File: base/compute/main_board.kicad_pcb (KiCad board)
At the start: 2 copper layers, 54.4 x 37.6 mm, 41 parts, among them J1 USB_C_Receptacle_USB2.0_16P, J2 Conn_01x20, J4 Conn_01x20, SW1 SW_Push_Open, U1 MCP1700T-1202ETT, U2 ESP32-S3-WROOM-2, U3 MCP1700T-3302E/TT, U4 W25X20CLSN, U5 ICE40UP5K-SG48ITR-FPGA_Lattice

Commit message: compute  module ready for fab
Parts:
- removed H3, H4: MountingHole, MountingHole:MountingHole_2.7mm_M2.5
- added H1: MountingHole, MountingHole:MountingHole_3.2mm_M3, F.Cu at (227.0, 139.0)
- added H2: MountingHole, MountingHole:MountingHole_3.2mm_M3, F.Cu at (200.0, 163.0)
- added SW2: SW_Push_Open, Button_Switch_SMD:SW_SPST_B3U-1000P, F.Cu at (192.6, 158.2)
- J1: footprint Connector_USB:USB_C_Receptacle_GCT_USB4105-xx-A_16P_TopMnt_Horizontal -> footprints:USB_C_Receptacle_GCT_USB4105-xx-A_16P_TopMnt_Horizontal
- J2, J4, U2: moved to F.Cu
- SW1: footprint footprints:SW_SPST_CK_KXT3 -> Button_Switch_SMD:SW_SPST_B3U-1000P
- U3: value MCP1700T-3302E/TT -> LD1117S33TR_SOT223; footprint Package_TO_SOT_SMD:SOT-23 -> Package_TO_SOT_SMD:SOT-223-3_TabPin2
- U5: footprint Package_DFN_QFN:QFN-48-1EP_7x7mm_P0.5mm_EP5.6x5.6mm -> footprints:QFN-48-1EP_7x7mm_P0.5mm_EP5.6x5.6mm
- moved C10 47.2 mm to (229.8, 155.8), turned to 90 degrees
- moved C2 47.0 mm to (226.7, 150.8), turned to 180 degrees
- moved U3 43.9 mm to (227.1, 162.6)
- moved C1 34.6 mm to (221.1, 161.9), turned to 0 degrees
- moved R10 32.5 mm to (206.5, 157.3)
- moved SW1 28.8 mm to (205.9, 137.8)
- moved U2 23.1 mm to (193.4, 145.4)
- moved C13 20.8 mm to (206.5, 155.2)
- moved R6 20.0 mm to (188.3, 161.0), turned to 0 degrees
- moved C14 18.9 mm to (206.5, 153.1)
- moved J1 17.2 mm to (181.1, 160.9)
- moved D2 16.8 mm to (212.8, 164.2)
- moved D3 15.5 mm to (191.1, 163.5)
- moved D1 14.4 mm to (207.8, 150.2), turned to 0 degrees
- moved U1 14.4 mm to (226.7, 153.7)
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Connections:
- C12 pad 1: +3V3 -> +3.3V
- C2 pad 1: +5V -> +3.3V
- C3 pad 1: +3V3 -> +3.3V
- C4 pad 1: +3V3 -> +3.3V
- C5 pad 1: +3V3 -> +3.3V
- C6 pad 1: +3V3 -> +3.3V
- C7 pad 1: +3V3 -> +3.3V
- C8 pad 1: +3V3 -> +3.3V
- D1 pad 2: +3V3 -> +3.3V
- D2 pad 1: +3V3 -> +3.3V
- J2 pad 10: SPI_SI -> HALL1
- J2 pad 11: SPI_SCK -> HALL2
- J2 pad 12: IC_HB_PWM1 -> HALL3
- J2 pad 13: IC_HB_PWM2 -> uH
- J2 pad 14: STEP_ENABLE -> uL
- J2 pad 15: POT_SCL -> vH
- J2 pad 16: POT_SDA -> vL
- J2 pad 17: FPGA36 -> wH
- J2 pad 18: FPGA37 -> wL
- J2 pad 19: FPGA46 -> IC_HB_PWM1
- J2 pad 2: uL -> POT_SDA
- J2 pad 20: FPGA48 -> IC_HB_PWM2
- J2 pad 3: uH -> POT_SCL
- J2 pad 4: vL -> GPIO21
- J2 pad 5: vL -> FPGA42
- J2 pad 6: wL -> FPGA43
- J2 pad 7: wH -> FPGA44
- J2 pad 8: SPI_SS_MOTOR -> FPGA46
- J2 pad 9: SPI_SO -> DIGITAL
- J4 pad 1: vH -> GND
- J4 pad 10: Z_PO -> SPI_SO
- J4 pad 11: Z_STEP -> SPI_SI
- J4 pad 12: Y_DIR -> Z_PO
- J4 pad 13: Y_PO -> Z_STEP
- J4 pad 14: Y_STEP -> Z_DIR
- J4 pad 15: X_DIR -> Y_PO
- J4 pad 16: X_PO -> Y_STEP
- J4 pad 17: X_STEP -> Y_DIR
- J4 pad 18: SPI_SO -> X_PO
- J4 pad 19: SPI_SI -> X_STEP
- J4 pad 2: HALL3 -> GPIO44
- J4 pad 20: GND -> X_DIR
- J4 pad 3: HALL1 -> GPIO43
- J4 pad 4: HALL2 -> FPGA41
- J4 pad 5: DIGITAL -> FPGA38
- J4 pad 6: FREE -> FPGA39
- J4 pad 7: FPGA51 -> STEP_ENABLE
- J4 pad 8: FPGA50 -> SPI_SS_MOTOR
- J4 pad 9: Z_DIR -> SPI_SCK
- R1 pad 1: +3V3 -> +3.3V
- R2 pad 1: +3V3 -> +3.3V
- R3 pad 2: +3V3 -> +3.3V
- R7 pad 1: +3V3 -> +3.3V
- U1 pad 3: +3V3 -> +3.3V
- U2 pad 12: unconnected-(U2-GPIO8/TOUCH8/ADC1_CH7/SUBSPICS1-Pad12) -> ESP32_RED
- U2 pad 15: unconnected-(U2-GPIO3/TOUCH3/ADC1_CH2-Pad15) -> FPGA41
- U2 pad 17: STEP_ENABLE -> SPI_SS_FPGA
- U2 pad 18: POT_SCL -> SPI_SS
- U2 pad 22: unconnected-(U2-GPIO14/TOUCH14/ADC2_CH3/FSPIWP/FSPIDQS/SUBSPIWP-Pad22) -> SPI_SS_MOTOR
- U2 pad 23: ESP32_RED -> GPIO21
- U2 pad 25: POT_SDA -> CFG_DONE
- U2 pad 26: SPI_SS_FPGA -> unconnected-(U2-GPIO45-Pad26)
- U2 pad 31: CFG_DONE -> STEP_ENABLE
- U2 pad 32: FREE -> unconnected-(U2-MTCK/GPIO39/CLK_OUT3/SUBSPICS1-Pad32)
- U2 pad 35: SPI_SS_MOTOR -> unconnected-(U2-MTMS/GPIO42-Pad35)
- U2 pad 36: unconnected-(U2-U0RXD/GPIO44/CLK_OUT2-Pad36) -> GPIO44
- U2 pad 37: Z_STEP -> GPIO43
- U2 pad 38: unconnected-(U2-GPIO2/TOUCH2/ADC1_CH1-Pad38) -> FPGA39
- U2 pad 39: unconnected-(U2-GPIO1/TOUCH1/ADC1_CH0-Pad39) -> FPGA38
- U2 pad 4: unconnected-(U2-GPIO4/TOUCH4/ADC1_CH3-Pad4) -> POT_SDA
- U2 pad 5: unconnected-(U2-GPIO5/TOUCH5/ADC1_CH4-Pad5) -> POT_SCL
- U2 pad 6: unconnected-(U2-GPIO6/TOUCH6/ADC1_CH5-Pad6) -> FPGA46
- U2 pad 7: unconnected-(U2-GPIO7/TOUCH7/ADC1_CH6-Pad7) -> FPGA44
- U2 pad 8: unconnected-(U2-GPIO15/U0RTS/ADC2_CH4/XTAL_32K_P-Pad8) -> FPGA42
- U2 pad 9: unconnected-(U2-GPIO16/U0CTS/ADC2_CH5/XTAL_32K_N-Pad9) -> FPGA43
- U4 pad 8: +3V3 -> +3.3V
- U5 pad 1: +3V3 -> +3.3V
- U5 pad 10: SPI_SS_FPGA -> Y_DIR
- U5 pad 11: Y_PO -> Y_STEP
- U5 pad 12: Y_STEP -> Y_PO
- U5 pad 20: Z_PO -> Z_DIR
- U5 pad 21: Y_DIR -> Z_STEP
- U5 pad 22: +3V3 -> +3.3V
- U5 pad 23: FPGA37 -> Z_PO
- U5 pad 25: FPGA36 -> SPI_SS_FPGA
- U5 pad 26: FREE -> FPGA39
- U5 pad 27: Z_STEP -> FPGA38
- U5 pad 28: Z_DIR -> FPGA41
- U5 pad 31: DIGITAL -> FPGA42
- U5 pad 32: HALL2 -> FPGA43
- U5 pad 33: +3V3 -> +3.3V
- U5 pad 34: HALL1 -> FPGA44
- U5 pad 36: FPGA48 -> DIGITAL
- U5 pad 37: HALL3 -> HALL1
- U5 pad 38: FPGA50 -> HALL2
- U5 pad 42: FPGA51 -> HALL3
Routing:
- net +3.3V: track 0.00 -> 149.1 mm, vias 0 -> 8
- net +3V3: track 123.5 -> 0.00 mm, vias 10 -> 0
- net +5V: track 0.00 -> 55.6 mm
- net FPGA44: track 0.00 -> 47.0 mm, vias 0 -> 1
- net FPGA41: track 0.00 -> 43.7 mm, vias 0 -> 1
- net FPGA43: track 0.00 -> 40.5 mm, vias 0 -> 2
- net FPGA38: track 0.00 -> 37.9 mm, vias 0 -> 1
- net FPGA39: track 0.00 -> 37.5 mm, vias 0 -> 1
- net FPGA42: track 0.00 -> 36.7 mm, vias 0 -> 2
- net FPGA46: track 14.9 -> 50.2 mm, vias 0 -> 1
- net GPIO21: track 0.00 -> 34.0 mm, vias 0 -> 1
- net X_STEP: track 0.00 -> 32.3 mm
- net +1V2: track 62.5 -> 30.8 mm
- net D+: track 0.00 -> 31.3 mm
- net X_PO: track 0.00 -> 30.9 mm
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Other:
- board size 54.4 x 37.6 mm -> 53.8 x 41.5 mm
- board text added: "BOOT"
- board text added: "EN"
- board text removed: "RASPBERRY-PI 40-PIN ADDON BOARD VIEW FROM TOP NOTE: P1 SHOULD BE FITTED ON THE REVERSE OF THE BOARD ADD EDGE CUTS FROM CAMERA AND DISPLAY PORTS AS REQUIRED"
- board text removed: "RJ45"
- board text removed: "USB"

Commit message: changes for extension
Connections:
- J2 pad 2: POT_SDA -> +3.3V
- J2 pad 3: POT_SCL -> POT_SDA
- J2 pad 4: GPIO21 -> POT_SCL
- U2 pad 23: GPIO21 -> unconnected-(U2-GPIO21-Pad23)
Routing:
- net GPIO21: track 34.0 -> 0.00 mm, vias 1 -> 0
- net +3.3V: track 149.1 -> 167.4 mm
- net POT_SDA: track 17.2 -> 16.4 mm
- net POT_SCL: track 16.3 -> 16.8 mm, vias 1 -> 2
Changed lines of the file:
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@@
 	(net 75 "GPIO43")
 	(net 76 "GPIO44")
-	(net 77 "GPIO21")
+	(net 77 "unconnected-(U2-GPIO21-Pad23)")
 	(footprint "Package_TO_SOT_SMD:SOT-23"
 		(layer "F.Cu")
@@
 			(size 1.5 0.9)
 			(layers "F.Cu" "F.Paste" "F.Mask")
-			(net 77 "GPIO21")
+			(net 77 "unconnected-(U2-GPIO21-Pad23)")
 			(pinfunction "GPIO21")
-			(pintype "bidirectional")
+			(pintype "bidirectional+no_connect")
 		)
 		(pad "24" smd rect
@@
 			(layers "*.Cu" "*.Mask")
 			(remove_unused_layers no)
-			(net 9 "POT_SDA")
+			(net 3 "+3.3V")
 			(pinfunction "Pin_2")
 			(pintype "passive")
@@
 			(layers "*.Cu" "*.Mask")
 			(remove_unused_layers no)
-			(net 11 "POT_SCL")
+			(net 9 "POT_SDA")
 			(pinfunction "Pin_3")
 			(pintype "passive")
@@
 			(layers "*.Cu" "*.Mask")
 			(remove_unused_layers no)
-			(net 77 "GPIO21")
+			(net 11 "POT_SCL")
 			(pinfunction "Pin_4")
 			(pintype "passive")
@@
 	)
 	(segment
+		(start 190.09 157.9)
+		(end 197.1375 157.9)
+		(width 0.25)
+		(layer "F.Cu")
+		(net 3)
+	)
+	(segment
 		(start 188.645 156.36061)
 		(end 188.645 157.44)
@@
 	)
 	(segment
+		(start 190.09 157.9)
+		(end 190.09 162.47061)
+		(width 0.25)
+		(layer "F.Cu")
+		(net 3)
+	)
+	(segment
+		(start 185.136555 166.403445)
+		(end 190.263445 166.403445)
+		(width 0.25)
+		(layer "F.Cu")
+		(net 3)
+	)
+	(segment
 		(start 206.4875 160.18)
 		(end 208.328626 160.18)
@@
 	)
 	(segment
+		(start 182.54 169)
+		(end 185.136555 166.403445)
+		(width 0.25)
+		(layer "F.Cu")
+		(net 3)
+	)
+	(segment
 		(start 220.0125 161.96)
 		(end 220.0125 164)
@@
 	)
 	(segment
+		(start 190.71 163.09061)
+		(end 190.71 165.95689)
+		(width 0.25)
+		(layer "F.Cu")
+		(net 3)
+	)
+	(segment
+		(start 190.71 165.95689)
+		(end 190.263445 166.403445)
+		(width 0.25)
+		(layer "F.Cu")
+		(net 3)
+	)
+	(segment
 		(start 219.5075 139.5)
 		(end 219.5075 139.46)
@@
 	)
 	(segment
+		(start 190.09 162.47061)
+		(end 190.71 163.09061)
+		(width 0.25)
+		(layer "F.Cu")
+		(net 3)
+	)
+	(segment
 		(start 214.0165 153.244526)
 		(end 214.0165 152.51)
@@
 	)
 	(segment
-		(start 189.105 157.9)
-		(end 197.1375 157.9)
-		(width 0.25)
-		(layer "F.Cu")
-		(net 3)
-	)
-	(segment
 		(start 214.0165 151.6535)
 		(end 213.5 151.137)
@@
 	)
 	(segment
+		(start 189.105 157.9)
+		(end 190.09 157.9)
+		(width 0.25)
+		(layer "F.Cu")
+		(net 3)
+	)
+	(segment
 		(start 228.1275 153.7375)
 		(end 228.07 153.68)
@@
 	)
 	(segment
+		(start 182.54 168.448652)
+		(end 183.127364 168.448652)
+		(width 0.25)
+		(layer "B.Cu")
+		(net 3)
+	)
+	(segment
 		(start 215.935 148.135)
 		(end 220.98 143.09)
@@
 	)
 	(segment
-		(start 182.54 168.448652)
-		(end 183.127364 168.448652)
+		(start 185.93 168.15)
+		(end 185.93 157.2)
 		(width 0.25)
 		(layer "B.Cu")
@@
 	)
 	(segment
-		(start 183.127364 168.448652)
-		(end 188.92 162.656016)
+		(start 185.08 169)
+		(end 185.93 168.15)
 		(width 0.25)
 		(layer "B.Cu")
@@
 	)
 	(segment
-		(start 188.92 162.656016)
+		(start 185.93 157.2)
 		(end 188.92 154.21)
 		(width 0.25)
@@
 		(net 10)
 	)
+	(segment
+		(start 186.63 166.98)
+		(end 186.63 168.01)
+		(width 0.25)
+		(layer "F.Cu")
+		(net 11)
+	)
+	(segment
+		(start 186.63 168.01)
+		(end 187.62 169)
+		(width 0.25)
+		(layer "F.Cu")
+		(net 11)
+	)
+	(via
+		(at 186.63 166.98)
+		(size 0.6)
+		(drill 0.4)
+		(layers "F.Cu" "B.Cu")
+		(net 11)
+	)
 	(via
 		(at 190.19 154.22)
@@
 	)
 	(segment
-		(start 185.08 168.448652)
-		(end 189.32 164.208652)
+		(start 186.63 166.9)
+		(end 186.63 166.98)
 		(width 0.25)
 		(layer "B.Cu")
@@
 	)
 	(segment
+		(start 189.32 164.208652)
+		(end 187.45 166.078652)
+		(width 0.25)
+		(layer "B.Cu")
+		(net 11)
+	)
+	(segment
+		(start 187.45 166.08)
+		(end 186.63 166.9)
+		(width 0.25)
+		(layer "B.Cu")
+		(net 11)
+	)
+	(segment
+		(start 186.63 166.98)
+		(end 186.55 166.98)
+		(width 0.25)
+		(layer "B.Cu")
+		(net 11)
+	)
+	(segment
+		(start 186.55 166.98)
+		(end 186.61 166.92)
+		(width 0.25)
+		(layer "B.Cu")
+		(net 11)
+	)
+	(segment
+		(start 187.45 166.078652)
+		(end 187.45 166.08)
+		(width 0.25)
+		(layer "B.Cu")
+		(net 11)
+	)
+	(segment
 		(start 215.66 140.65)
 		(end 212.505686 140.65)
@@
 	)
 	(segment
-		(start 189.4025 166.015)
+		(start 189.414055 166.003445)
 		(end 189.8775 165.54)
 		(width 0.25)
@@
 	(segment
 		(start 180 168.448652)
-		(end 182.433652 166.015)
+		(end 182.445207 166.003445)
 		(width 0.25)
 		(layer "F.Cu")
@@
 	)
 	(segment
-		(start 182.433652 166.015)
-		(end 189.4025 166.015)
+		(start 182.445207 166.003445)
+		(end 189.414055 166.003445)
 		(width 0.25)
 		(layer "F.Cu")
@@
 	(segment
 		(start 187.559009 170.53)
-		(end 186.495 169.465991)
+		(end 196.25 170.53)
 		(width 0.25)
 		(layer "B.Cu")
@@
 	)
 	(segment
-		(start 197.78 169)
-		(end 196.25 170.53)
+		(start 189.72 155.874952)
+		(end 189.72 164.434314)
 		(width 0.25)
 		(layer "B.Cu")
@@
 	)
 	(segment
-		(start 186.495 167.620685)
-		(end 189.72 164.395685)
+		(start 189.74 164.454314)
+		(end 189.74 165.289009)
 		(width 0.25)
 		(layer "B.Cu")
@@
 	)
 	(segment
-		(start 189.72 164.395685)
-		(end 189.72 155.874952)
+		(start 186.495 169.465991)
+		(end 187.559009 170.53)
+		(width 0.25)
+		(layer "B.Cu")
+		(net 65)
+	)
+	(segment
+		(start 186.495 168.534009)
+		(end 186.495 169.465991)
 		(width 0.25)
 		(layer "B.Cu")
@@
 	(segment
 		(start 196.25 170.53)
-		(end 187.559009 170.53)
+		(end 197.78 169)
 		(width 0.25)
 		(layer "B.Cu")
@@
 	)
 	(segment
-		(start 189.72 155.874952)
-		(end 191.347842 154.24711)
+		(start 189.72 164.434314)
+		(end 189.74 164.454314)
 		(width 0.25)
 		(layer "B.Cu")
@@
 	)
 	(segment
-		(start 186.495 169.465991)
-		(end 186.495 167.620685)
+		(start 189.74 165.289009)
+		(end 186.495 168.534009)
+		(width 0.25)
+		(layer "B.Cu")
+		(net 65)
+	)
+	(segment
+		(start 191.347842 154.24711)
+		(end 189.72 155.874952)
 		(width 0.25)
 		(layer "B.Cu")
@@
 		(net 76)
 	)
-	(segment
-		(start 195.83 148.23)
-		(end 195.8 148.21)
-		(width 0.25)
-		(layer "F.Cu")
-		(net 77)
-	)
-	(segment
-		(start 201.37 142.235)
-		(end 195.8 147.805)
-		(width 0.25)
-		(layer "F.Cu")
-		(net 77)
-	)
-	(segment
-		(start 195.8 147.805)
-		(end 195.83 148.23)
-		(width 0.25)
-		(layer "F.Cu")
-		(net 77)
-	)
-	(segment
-		(start 202.88 142.235)
-		(end 201.37 142.235)
-		(width 0.25)
-		(layer "F.Cu")
-		(net 77)
-	)
-	(via
-		(at 195.83 148.23)
-		(size 0.6)
-		(drill 0.4)
-		(layers "F.Cu" "B.Cu")
-		(net 77)
-	)
-	(segment
-		(start 192.526587 164.093413)
-		(end 192.526587 151.533413)
-		(width 0.25)
-		(layer "B.Cu")
-		(net 77)
-	)
-	(segment
-		(start 192.526587 151.533413)
-		(end 195.83 148.23)
-		(width 0.25)
-		(layer "B.Cu")
-		(net 77)
-	)
-	(segment
-		(start 187.62 169)
-		(end 192.526587 164.093413)
-		(width 0.25)
-		(layer "B.Cu")
-		(net 77)
-	)
 	(zone

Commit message: improved layout main board
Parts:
- added R8: 10K, Resistor_SMD:R_0805_2012Metric, F.Cu at (192.2, 155.0)
- added R9: 10K, Resistor_SMD:R_0805_2012Metric, F.Cu at (192.2, 157.2)
- G1: moved to F.Cu
- moved SW2 45.1 mm to (234.5, 141.6), turned to 0 degrees
- moved D4 35.4 mm to (235.5, 153.9), turned to -90 degrees
- moved D2 29.3 mm to (235.5, 145.6), turned to -90 degrees
- moved SW1 28.6 mm to (234.5, 137.8), turned to 0 degrees
- moved H2 26.1 mm to (174.5, 168.5)
- moved C10 11.6 mm to (226.9, 167.0), turned to 180 degrees
- moved H1 10.3 mm to (234.0, 131.5)
- moved R4 9.70 mm to (188.4, 155.0), turned to 180 degrees
- moved G1 8.46 mm to (205.6, 133.8), turned to 0 degrees
- moved U2 7.16 mm to (187.1, 142.0)
- moved J1 6.53 mm to (174.7, 159.3)
- moved F2 6.44 mm to (188.7, 163.8)
- moved C9 6.29 mm to (182.4, 155.0)
- moved D3 6.29 mm to (185.1, 161.8)
- moved D5 6.29 mm to (185.1, 163.9)
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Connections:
- C11 pad 1: +3.3V -> +1V2
- J2 pad 2: +3.3V -> GPIO46
- J2 pad 5: FPGA42 -> FPGA44
- J2 pad 6: FPGA43 -> FPGA42
- J2 pad 7: FPGA44 -> FPGA43
- U2 pad 16: unconnected-(U2-GPIO46-Pad16) -> GPIO46
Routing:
- net Net-(U2-EN): track 12.2 -> 76.0 mm, vias 0 -> 2
- net ESP32_BLUE: track 4.83 -> 56.1 mm, vias 0 -> 2
- net ESP32_GREEN: track 4.76 -> 53.4 mm, vias 0 -> 2
- net ESP32_RED: track 6.32 -> 52.1 mm, vias 0 -> 2
- net FPGAG: track 4.43 -> 47.5 mm, vias 0 -> 2
- net Net-(U2-GPIO0/BOOT): track 4.51 -> 47.2 mm
- net GPIO46: track 0.00 -> 36.9 mm, vias 0 -> 1
- net FPGAB: track 3.91 -> 39.6 mm, vias 0 -> 2
- net FPGAR: track 8.13 -> 33.3 mm, vias 0 -> 2
- net POT_SCL: track 16.8 -> 35.8 mm, vias 2 -> 1
- net POT_SDA: track 16.4 -> 33.1 mm
- net SPI_SS_MOTOR: track 20.6 -> 10.8 mm
- net FPGA41: track 43.7 -> 52.7 mm
- net FPGA38: track 37.9 -> 46.3 mm
- net FPGA43: track 40.5 -> 48.8 mm
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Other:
- board size 53.8 x 41.5 mm -> 66.5 x 44 mm
- board text added: "ESP32"
- board text added: "FPGA"
- board text added: "version 0.1"

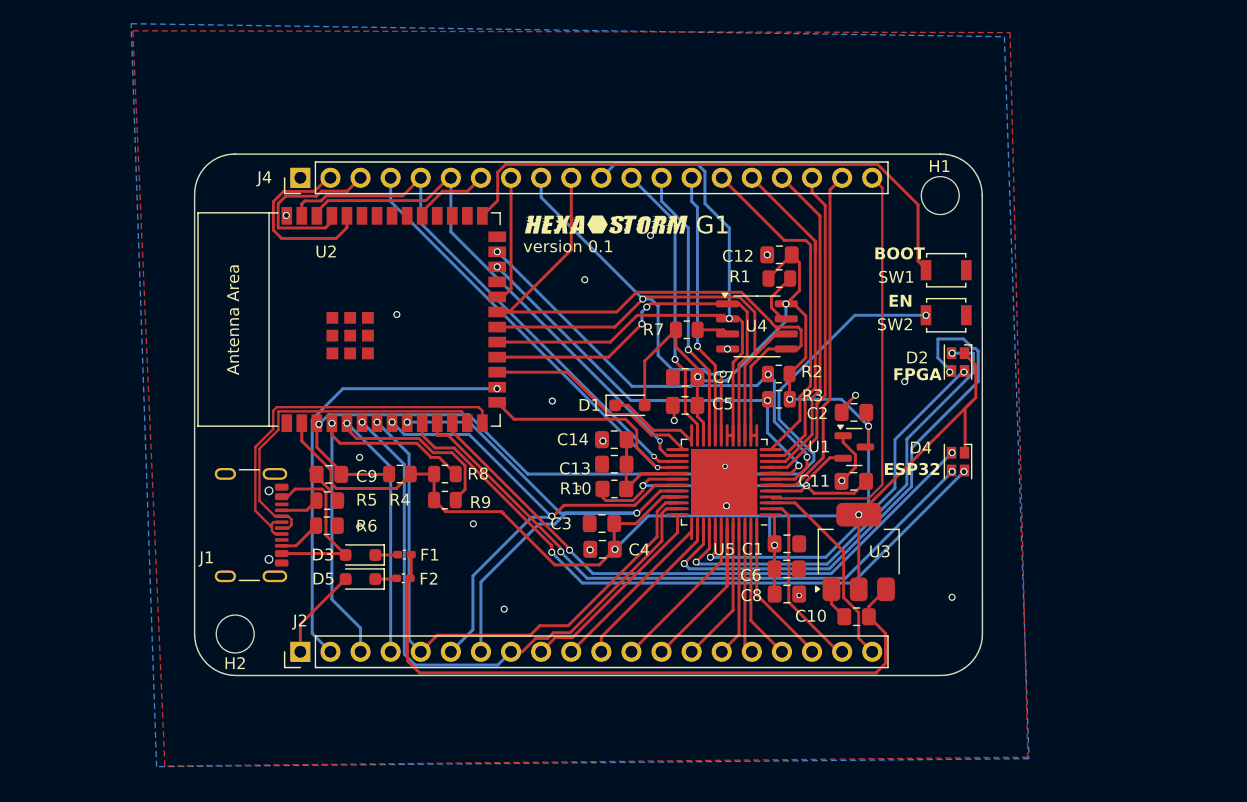
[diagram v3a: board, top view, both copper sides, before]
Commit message: moved from 2 headers to 1 smt 40 pin header
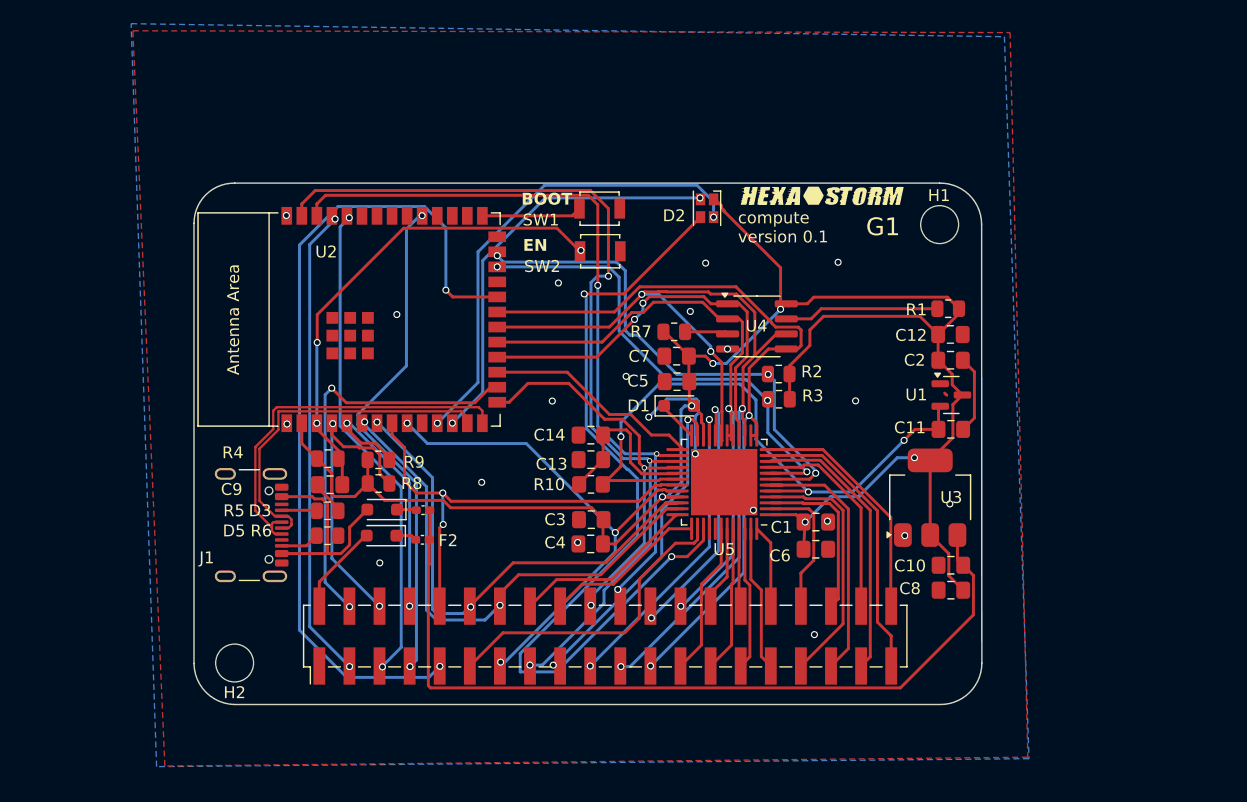
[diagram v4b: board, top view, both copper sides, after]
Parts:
- removed D4: LED_ABGR, footprints:LED_Cree-PLCC4_2x2mm_CW
- removed J2, J4: Conn_01x20, Connector_PinHeader_2.54mm:PinHeader_1x20_P2.54mm_Vertical
- added J3: Conn_02x20_Counter_Clockwise, Connector_PinHeader_2.54mm:PinHeader_2x20_P2.54mm_Vertical_SMD, F.Cu at (205.7, 168.7)
- moved SW1 29.7 mm to (205.2, 132.6)
- moved SW2 29.7 mm to (205.3, 136.2)
- moved D2 24.8 mm to (214.3, 132.6)
- moved G1 18.4 mm to (223.8, 131.4)
- moved C12 15.9 mm to (234.9, 143.2), turned to 0 degrees
- moved R1 14.5 mm to (234.7, 141.0), turned to 180 degrees
- moved C8 13.8 mm to (234.9, 164.8), turned to 180 degrees
- moved C11 9.29 mm to (234.9, 151.2), turned to 0 degrees
- moved U1 9.29 mm to (234.9, 148.3)
- moved C2 9.27 mm to (234.9, 145.4), turned to 0 degrees
- moved C10 9.07 mm to (234.9, 162.7)
- moved U3 7.57 mm to (233.2, 157.0)
- moved R9 6.56 mm to (186.6, 153.8)
- moved R4 6.22 mm to (182.3, 153.7), turned to 0 degrees
- moved R8 5.66 mm to (186.6, 155.8)
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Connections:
- D2 pad 2: FPGAR -> ESP32_BLUE
- D2 pad 4: FPGAB -> ESP32_RED
- U2 pad 10: ESP32_BLUE -> unconnected-(U2-GPIO17/U1TXD/ADC2_CH6-Pad10)
- U2 pad 11: ESP32_GREEN -> ESP32_BLUE
- U5 pad 40: FPGAB -> unconnected-(U5A-RGB1-Pad40)
- U5 pad 41: FPGAR -> unconnected-(U5A-RGB2-Pad41)
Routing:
- net SPI_SS_MOTOR: track 10.8 -> 71.1 mm, vias 0 -> 2
- net ESP32_GREEN: track 53.4 -> 0.00 mm, vias 2 -> 0
- net FPGAB: track 39.6 -> 0.00 mm, vias 2 -> 0
- net Net-(U2-GPIO0/BOOT): track 47.2 -> 8.44 mm
- net STEP_ENABLE: track 6.49 -> 43.8 mm, vias 0 -> 2
- net Net-(U2-EN): track 76.0 -> 41.6 mm, vias 2 -> 3
- net FPGAR: track 33.3 -> 0.00 mm, vias 2 -> 0
- net FPGA38: track 46.3 -> 78.6 mm, vias 1 -> 3
- net GPIO43: track 14.7 -> 40.1 mm, vias 0 -> 2
- net GPIO44: track 15.9 -> 41.0 mm, vias 0 -> 2
- net FPGAG: track 47.5 -> 71.8 mm
- net FPGA39: track 45.5 -> 65.4 mm, vias 1 -> 3
- net +1V2: track 36.6 -> 54.9 mm, vias 2 -> 3
- net FPGA41: track 52.7 -> 34.4 mm, vias 1 -> 2
- net ESP32_RED: track 52.1 -> 35.3 mm
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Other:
- board text added: "compute version 0.1"
- board text removed: "ESP32"
- board text removed: "FPGA"
- board text removed: "version 0.1"
